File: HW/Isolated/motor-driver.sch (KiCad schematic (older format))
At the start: 42 parts

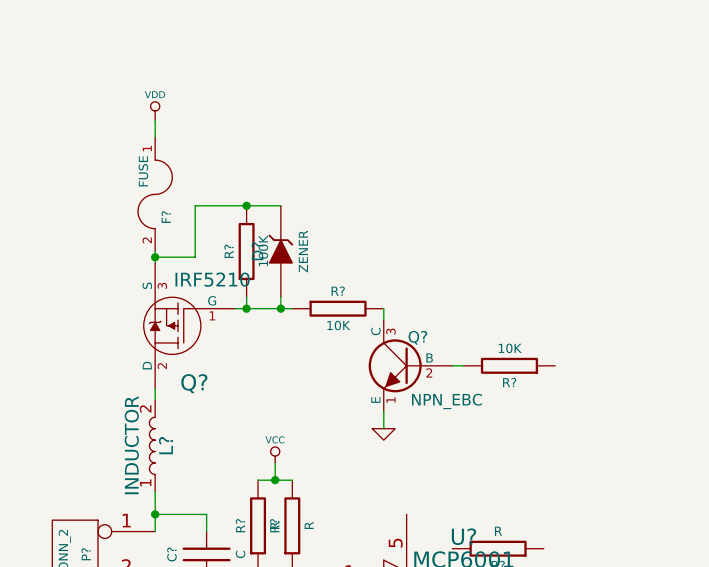
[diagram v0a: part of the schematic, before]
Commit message: Symulation added
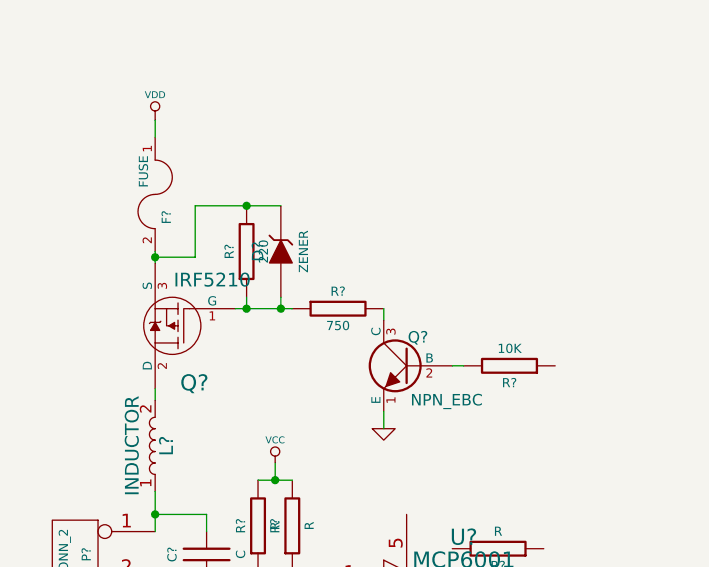
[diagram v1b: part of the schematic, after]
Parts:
- R?: value 100K -> 220
- R?: value 10K -> 750
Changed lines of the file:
@@
 Sheet 1 1
 Title ""
-Date "17 jan 2015"
+Date "19 jan 2015"
 Rev ""
 Comp ""
@@
 P 1800 3950
 F 0 "R?" H 1800 3875 40  0000 C CNN
-F 1 "100K" H 1800 4025 40  0000 C CNN
+F 1 "220" H 1800 4025 40  0000 C CNN
 F 2 "~" H 1800 3950 60  0000 C CNN
 F 3 "~" H 1800 3950 60  0000 C CNN
@@
 P 2200 4200
 F 0 "R?" H 2200 4125 40  0000 C CNN
-F 1 "10K" H 2200 4275 40  0000 C CNN
+F 1 "750" H 2200 4275 40  0000 C CNN
 F 2 "~" H 2200 4200 60  0000 C CNN
 F 3 "~" H 2200 4200 60  0000 C CNN

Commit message: Schematic changed
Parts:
- removed C?: 10uF/25V, C1P_D2, symbol CP
- removed D?: LED, LED3, symbol LED
- removed D?: BZX55C15, D3, symbol ZENER
- removed P?: IN+, HEADER_6.3, symbol CONN_1
- removed P?: OUT+, HEADER_6.3, symbol CONN_1
- removed P?: OUT-, HEADER_6.3, symbol CONN_1
- removed P?: IN-, HEADER_6.3, symbol CONN_1
- removed P?: LED, HDR-2, symbol CONN_2
- removed P?: SW_IN, HDR-2, symbol CONN_2
- removed P?: SENSE, HDR-2, symbol CONN_2
- removed Q?: NPN_EBC, ~, symbol NPN_EBC
- removed R?: 10R, R4, symbol R
- removed R? (x2): 100K, R4, symbol R
- removed R? (x2): 10K, R4, symbol R
- removed R?: 6K8 (48V), R4, symbol R
- removed R?: 220, ~, symbol R
- removed U?: INA168, SOT23-5, symbol INA168
- added C?: 1000uF/63V, ~, symbol CP
- added D?: DIODESCH, symbol DIODESCH
- added Q? (x2): BC546B, TO-92, symbol NPN_CBE
- added R?: 1, R4, symbol R
- added R?: 750, R6, symbol R
- added R?: 100, R4, symbol R
- C?: value C -> 1uF/63V
- L?: value INDUCTOR -> 22uH/10A
- R? (x2): value R -> 220K; footprint ~ -> R4
- R? (x2): value R -> 10K; footprint ~ -> R4
- R?: value 750 -> 750/2W; footprint ~ -> R6
- R?: value 10K -> 1K8; footprint ~ -> R4
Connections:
- wire segments 77 -> 53
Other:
- moved on the sheet: C?, D?, F?, L?, Q?, R?, U?

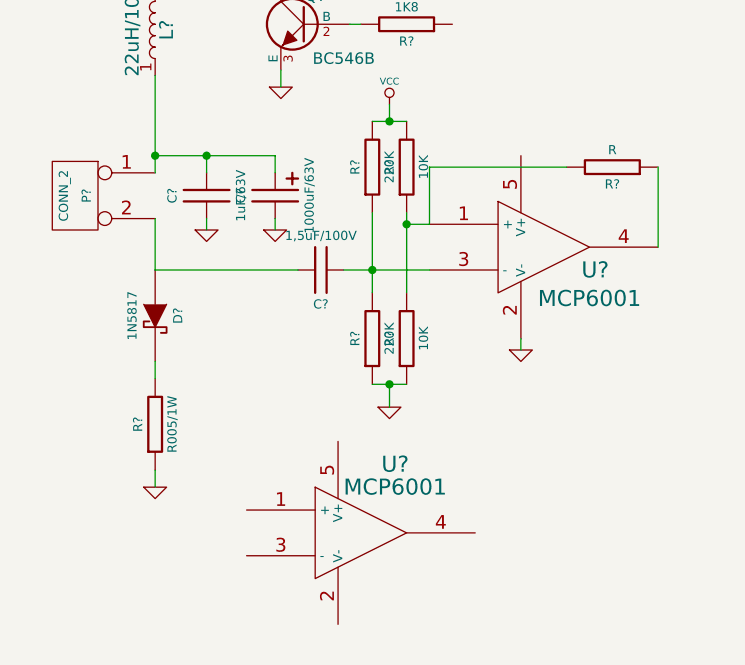
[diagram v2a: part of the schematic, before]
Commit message: Schematic modified - changed to MCP6002
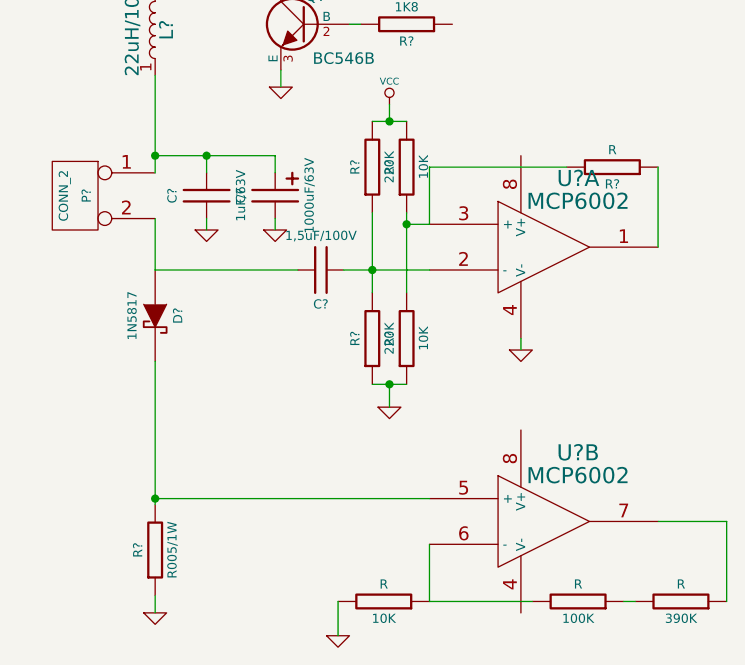
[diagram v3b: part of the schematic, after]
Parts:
- removed U? (x2): MCP6001, ~, symbol MCP6001
- added 100K, 10K, 390K: R, ~, symbol R
- added U? (x2): MCP6002, ~, symbol MCP6002
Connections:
- net GND: now also 10K.1, U?.4 (V-)
- net at D?.2 (K), R?.1: now also U?.5 (+)
- net at R?.1, R?.1, R?.2: now also U?.3 (+)
- net at C?.2, R?.1, R?.2: now also U?.2 (-)
- net at R?.2: now also U?.1
- new net: 100K.1, 10K.2, U?.6 (-)
- new net: 390K.2, U?.7
- new net: 100K.2, 390K.1
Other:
- moved on the sheet: R?
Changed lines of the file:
@@
 Sheet 1 1
 Title ""
-Date "24 jan 2015"
+Date "26 jan 2015"
 Rev ""
 Comp ""
@@
 L R R?
 U 1 1 54950B2A
-P 1400 6275
-F 0 "R?" H 1400 6200 40  0000 C CNN
-F 1 "R005/1W" H 1400 6350 40  0000 C CNN
-F 2 "R4_5_6" H 1400 6275 60  0001 C CNN
-F 3 "~" H 1400 6275 60  0000 C CNN
-	1    1400 6275
+P 1400 6825
+F 0 "R?" H 1400 6750 40  0000 C CNN
+F 1 "R005/1W" H 1400 6900 40  0000 C CNN
+F 2 "R4_5_6" H 1400 6825 60  0001 C CNN
+F 3 "~" H 1400 6825 60  0000 C CNN
+	1    1400 6825
 	0    1    1    0
 $EndComp
@@
 L GND #PWR?
 U 1 1 549513A5
-P 1400 6550
-F 0 "#PWR?" H 1400 6550 30  0001 C CNN
-F 1 "GND" H 1400 6480 30  0001 C CNN
-F 2 "" H 1400 6550 60  0000 C CNN
-F 3 "" H 1400 6550 60  0000 C CNN
-	1    1400 6550
+P 1400 7100
+F 0 "#PWR?" H 1400 7100 30  0001 C CNN
+F 1 "GND" H 1400 7030 30  0001 C CNN
+F 2 "" H 1400 7100 60  0000 C CNN
+F 3 "" H 1400 7100 60  0000 C CNN
+	1    1400 7100
 	1    0    0    -1
 $EndComp
@@
 	-1   0    0    -1
 $EndComp
-$Comp
-L MCP6001 U?
-U 1 1 54952A79
-P 2300 6750
-F 0 "U?" H 2450 7050 70  0000 C CNN
-F 1 "MCP6001" H 2450 6950 70  0000 C CNN
-F 2 "~" H 2300 6750 60  0000 C CNN
-F 3 "~" H 2300 6750 60  0000 C CNN
-	1    2300 6750
-	1    0    0    -1
-$EndComp
-$Comp
-L MCP6001 U?
-U 1 1 54952A88
-P 3100 5500
-F 0 "U?" H 3325 5400 70  0000 C CNN
-F 1 "MCP6001" H 3300 5275 70  0000 C CNN
-F 2 "~" H 3100 5500 60  0000 C CNN
-F 3 "~" H 3100 5500 60  0000 C CNN
-	1    3100 5500
-	1    0    0    -1
-$EndComp
 Wire Wire Line
 	1400 5375 1400 5600
 Wire Wire Line
-	1400 6000 1400 6075
-Wire Wire Line
-	1400 6475 1400 6550
+	1400 6000 1400 6625
+Wire Wire Line
+	1400 7025 1400 7100
 $Comp
 L INDUCTOR L?
@@
 	3425 4275 3425 3950
 Connection ~ 1950 4275
+$Comp
+L MCP6002 U?
+U 1 1 54C67B76
+P 3100 5500
+F 0 "U?" H 3250 5800 70  0000 C CNN
+F 1 "MCP6002" H 3250 5700 70  0000 C CNN
+F 2 "~" H 3100 5500 60  0000 C CNN
+F 3 "~" H 3100 5500 60  0000 C CNN
+	1    3100 5500
+	1    0    0    -1
+$EndComp
+$Comp
+L MCP6002 U?
+U 2 1 54C67B85
+P 3100 6700
+F 0 "U?" H 3250 7000 70  0000 C CNN
+F 1 "MCP6002" H 3250 6900 70  0000 C CNN
+F 2 "~" H 3100 6700 60  0000 C CNN
+F 3 "~" H 3100 6700 60  0000 C CNN
+	2    3100 6700
+	1    0    0    -1
+$EndComp
+Wire Wire Line
+	2600 6600 1400 6600
+Connection ~ 1400 6600
+$Comp
+L R 390K
+U 1 1 54C67C2A
+P 3700 7050
+F 0 "390K" H 3700 6975 40  0000 C CNN
+F 1 "R" H 3700 7125 40  0000 C CNN
+F 2 "~" H 3700 7050 60  0000 C CNN
+F 3 "~" H 3700 7050 60  0000 C CNN
+	1    3700 7050
+	1    0    0    -1
+$EndComp
+$Comp
+L R 10K
+U 1 1 54C67C39
+P 2400 7050
+F 0 "10K" H 2400 6975 40  0000 C CNN
+F 1 "R" H 2400 7125 40  0000 C CNN
+F 2 "~" H 2400 7050 60  0000 C CNN
+F 3 "~" H 2400 7050 60  0000 C CNN
+	1    2400 7050
+	1    0    0    -1
+$EndComp
+Wire Wire Line
+	2600 6800 2600 7050
+$Comp
+L GND #PWR?
+U 1 1 54C67D32
+P 2200 7200
+F 0 "#PWR?" H 2200 7200 30  0001 C CNN
+F 1 "GND" H 2200 7130 30  0001 C CNN
+F 2 "" H 2200 7200 60  0000 C CNN
+F 3 "" H 2200 7200 60  0000 C CNN
+	1    2200 7200
+	1    0    0    -1
+$EndComp
+Wire Wire Line
+	2200 7050 2200 7200
+$Comp
+L R 100K
+U 1 1 54C67DB6
+P 3250 7050
+F 0 "100K" H 3250 6975 40  0000 C CNN
+F 1 "R" H 3250 7125 40  0000 C CNN
+F 2 "~" H 3250 7050 60  0000 C CNN
+F 3 "~" H 3250 7050 60  0000 C CNN
+	1    3250 7050
+	1    0    0    -1
+$EndComp
+Wire Wire Line
+	3600 6700 3900 6700
+Wire Wire Line
+	3900 6700 3900 7050
+Wire Wire Line
+	3500 7050 3450 7050
+Wire Wire Line
+	2600 7050 3050 7050
 $EndSCHEMATC
